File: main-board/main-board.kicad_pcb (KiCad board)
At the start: 4 copper layers, 142.9 x 86.4 mm, 175 parts, among them J1 BOOT, J10 8P8CDouble, J11 Qwiic, J12 Qwiic, J13 Qwiic, J14 YELLOW, J15 GREEN, J2 USB Header, J3 JTAG, J4 5V Input, J5 StatusPanel, J6 Magjack, J7 8P8CDouble, J8 8P8CDouble, J9 8P8CDouble, Q1 N Channel, Q10 N Channel, Q11 N Channel, Q12 N Channel, Q13 P Channel, Q14 P Channel, Q15 P Channel, Q16 P Channel, Q17 P Channel, Q2 N Channel, Q3 N Channel, Q4 N Channel, Q5 P Channel, Q6 P Channel, Q7 P Channel, Q8 P Channel, Q9 N Channel, U1 STM32H743ZITx, U10 ISL83490, U11 ISL83490, U12 ISL83490, U2 USBLC6-2SC6, U3 3.3V Reg, U4 KSZ8041MLL, U5 ISL83490, U6 ISL83490, U7 ISL83490, U8 ISL83490, U9 ISL83490, X1 20MHz Oscillator, X2 25MHz Oscillator

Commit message: Swap power filter caps, tighten up trace routing
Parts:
- C47: footprint Capacitors_SMD:CP_Elec_5x4.5 -> Capacitors_SMD:CP_Elec_4x4.5
- C48: footprint Capacitors_SMD:CP_Elec_4x4.5 -> Capacitors_SMD:CP_Elec_5x5.3
- moved C1 17.1 mm to (154.7, 109.5)
- moved R50 3.90 mm to (198.8, 130.6)
- moved R51 3.90 mm to (198.8, 126.5)
- moved J14 3.90 mm to (203.3, 129.5)
- moved J15 3.90 mm to (203.3, 125.9)
- moved C29 3.34 mm to (202.3, 122.4), turned to 180 degrees
- moved J6 1.78 mm to (198.9, 115.6)
- moved C3 1.52 mm to (145.0, 106.2)
- moved C31 1.40 mm to (197.4, 123.6)
- moved FB5 1.40 mm to (194.3, 121.3)
- moved C30 1.40 mm to (197.4, 121.4)
- moved C25 0.99 mm to (167.4, 114.2)
- moved FB3 0.99 mm to (165.1, 114.2)
- moved C2 0.89 mm to (141.4, 106.2)
- moved FB2 0.18 mm to (181.2, 121.8)
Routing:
- net /I2C2_SDA: track 83.1 -> 69.3 mm
- net Net-(C30-Pad1): track 16.1 -> 24.7 mm
- net /JACK_YEL_CATH: track 18.1 -> 23.9 mm
- net /ETH_TXD0: track 53.3 -> 48.5 mm
- net /UART7_RX: track 42.1 -> 46.3 mm
- net /I2C2_SCL: track 72.0 -> 76.0 mm
- net /VBUS_SENSE: track 67.3 -> 71.0 mm, vias 0 -> 2
- net GND: track 329.3 -> 325.9 mm, vias 60 -> 58
- net /LINK2_Y: track 20.0 -> 22.8 mm
- net +3V3: track 86.1 -> 83.6 mm, vias 24 -> 23
- net /JACK_GRN_CATH: track 11.6 -> 9.20 mm
- net Net-(C32-Pad1): track 9.83 -> 7.97 mm
- net /ETH_LED0: track 31.2 -> 29.4 mm, vias 2 -> 0
- net /ETH_RD-: track 18.5 -> 20.3 mm
- net /ETH_TXD1: track 52.5 -> 50.8 mm
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
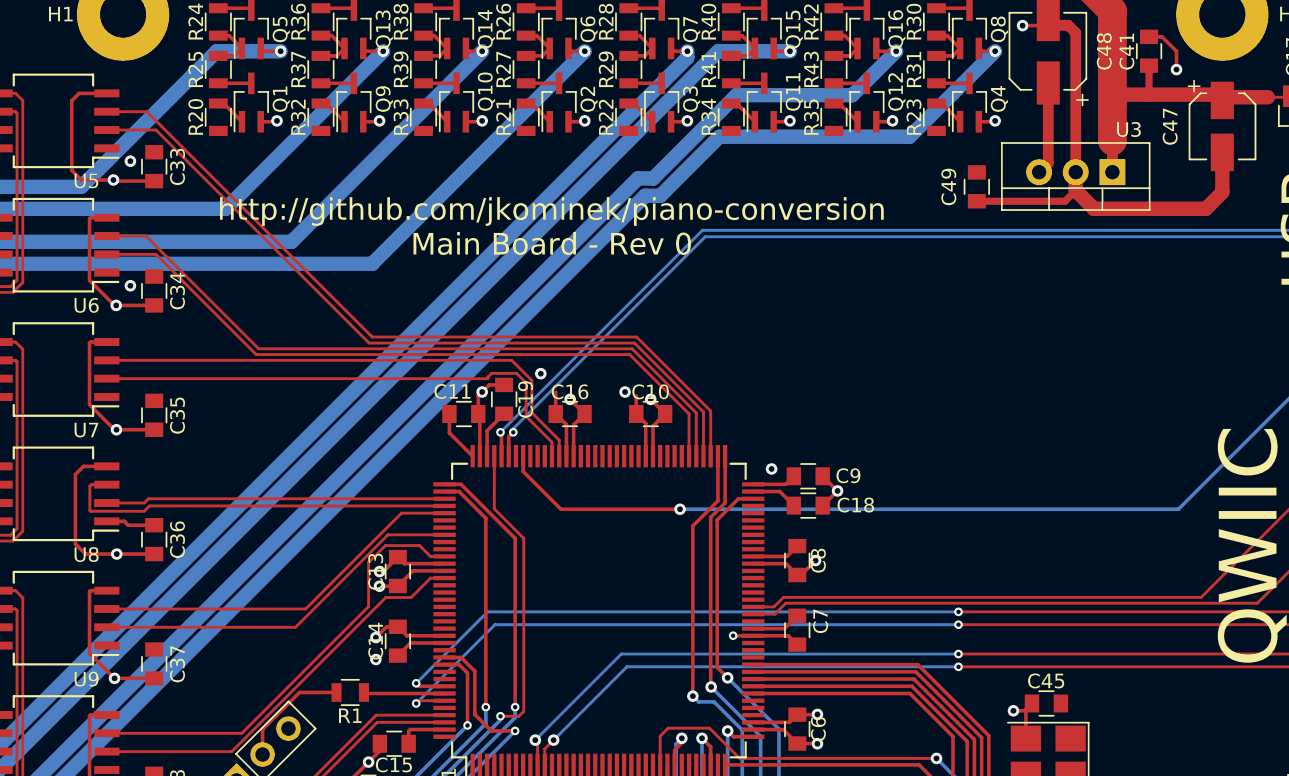
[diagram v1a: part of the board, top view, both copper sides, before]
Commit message: GPIO control lines for the MOSFET array
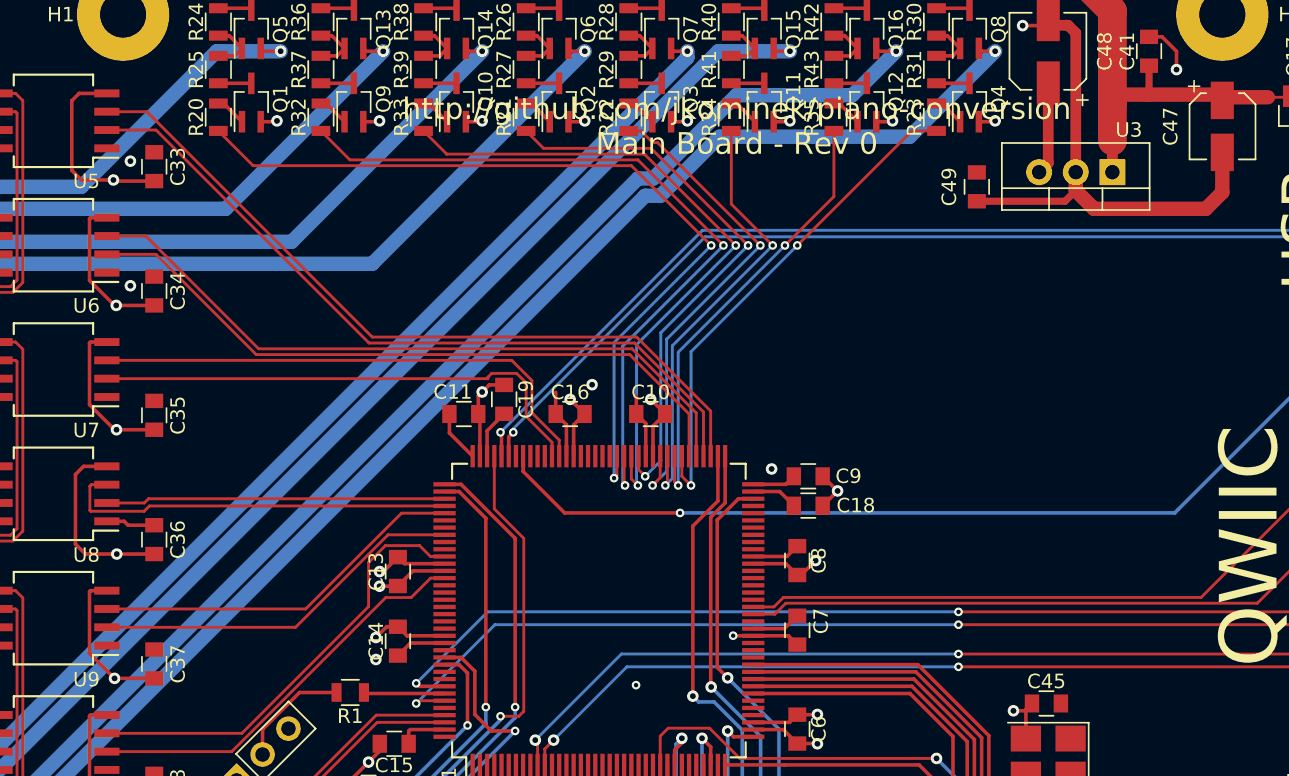
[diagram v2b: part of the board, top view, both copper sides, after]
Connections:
- R20 pad 2: (no net) -> /PWR1_CTRL
- R21 pad 2: (no net) -> /PWR3_CTRL
- R22 pad 2: (no net) -> /PWR5_CTRL
- R23 pad 2: (no net) -> /PWR7_CTRL
- R32 pad 2: (no net) -> /PWR2_CTRL
- R33 pad 2: (no net) -> /PWR4_CTRL
- R34 pad 2: (no net) -> /PWR6_CTRL
- R35 pad 2: (no net) -> /PWR8_CTRL
- U1 pad 79: (no net) -> /PWR7_CTRL
- U1 pad 80: (no net) -> /PWR8_CTRL
- U1 pad 81: (no net) -> /PWR6_CTRL
- U1 pad 82: (no net) -> /PWR5_CTRL
- U1 pad 85: (no net) -> /PWR3_CTRL
- U1 pad 86: (no net) -> /PWR4_CTRL
- U1 pad 87: (no net) -> /PWR2_CTRL
- U1 pad 88: (no net) -> /PWR1_CTRL
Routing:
- net /PWR1_CTRL: track 0.00 -> 58.0 mm, vias 0 -> 2
- net /PWR2_CTRL: track 0.00 -> 53.2 mm, vias 0 -> 2
- net /PWR4_CTRL: track 0.00 -> 46.7 mm, vias 0 -> 2
- net /PWR3_CTRL: track 0.00 -> 39.2 mm, vias 0 -> 2
- net /PWR7_CTRL: track 0.00 -> 34.9 mm, vias 0 -> 2
- net /PWR5_CTRL: track 0.00 -> 34.4 mm, vias 0 -> 2
- net /PWR8_CTRL: track 0.00 -> 31.2 mm, vias 0 -> 2
- net /PWR6_CTRL: track 0.00 -> 30.9 mm, vias 0 -> 2
- net GND: vias 58 -> 59
- net +3V3: vias 23 -> 22

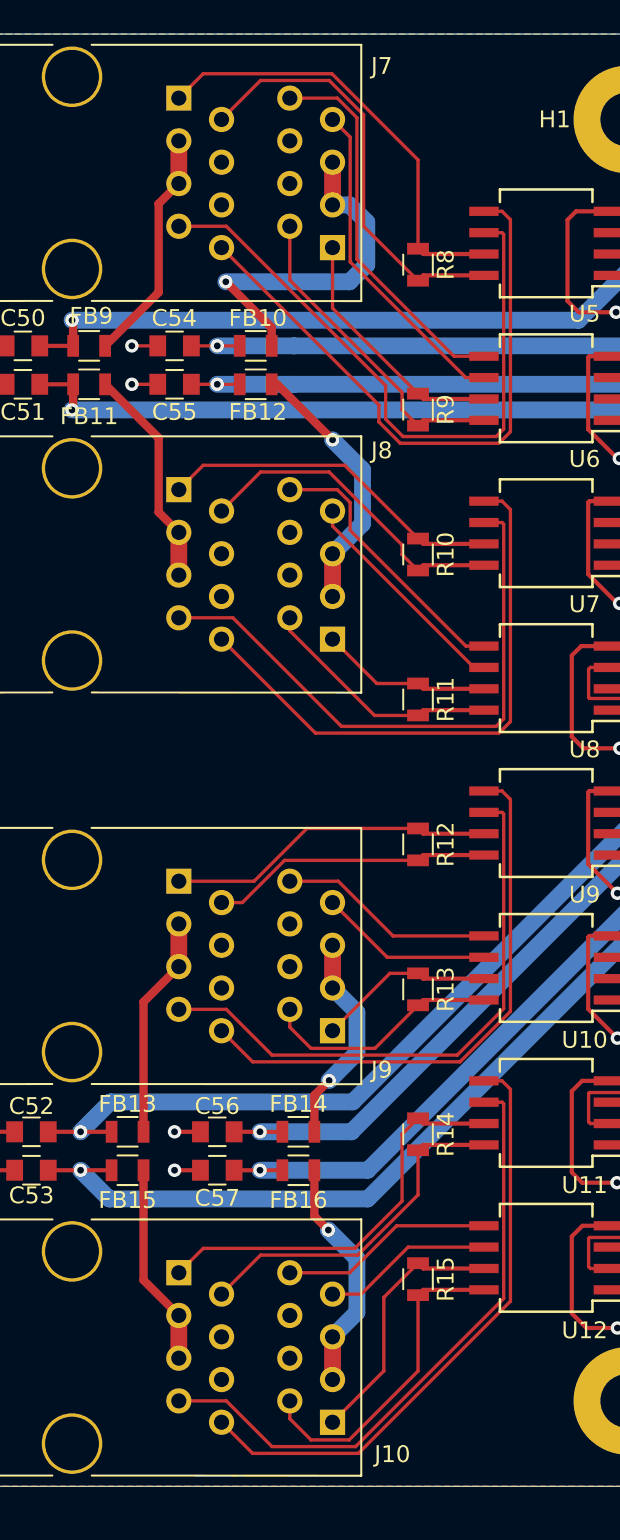
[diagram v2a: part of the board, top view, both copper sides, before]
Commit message: Correct RS485 Z/Y pin swap
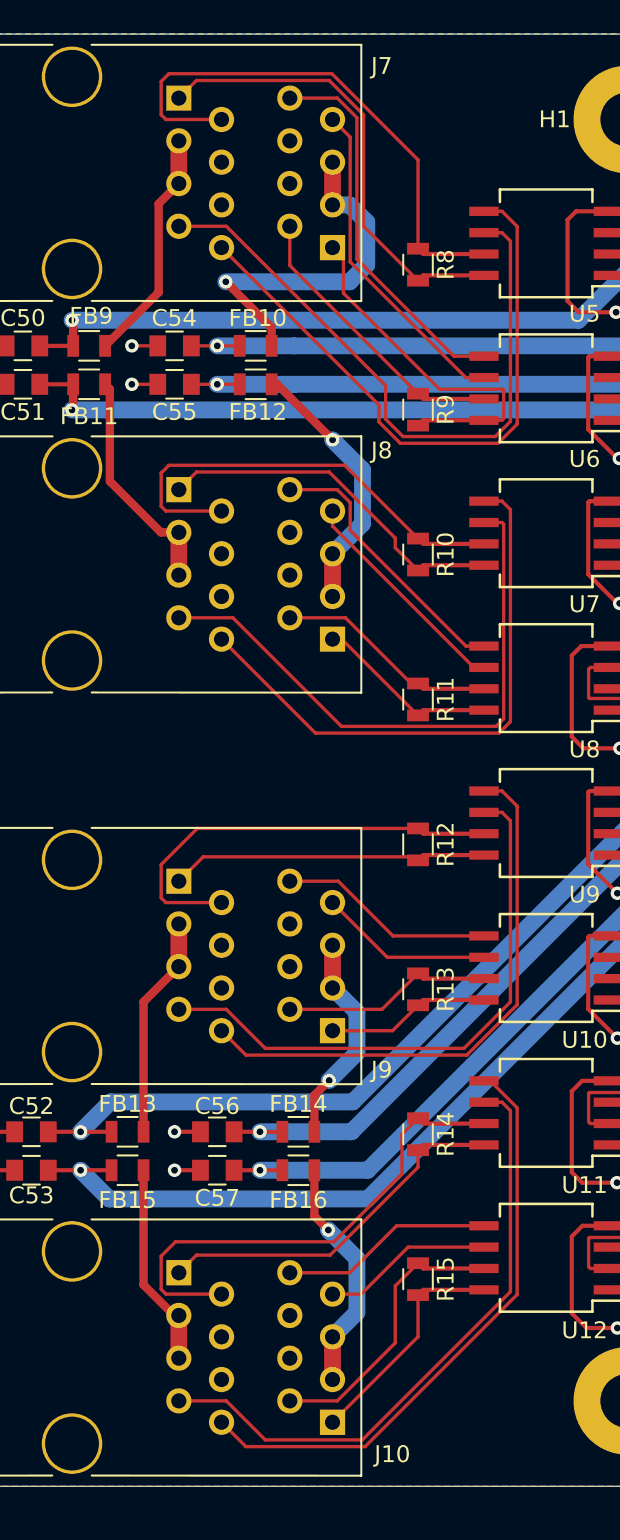
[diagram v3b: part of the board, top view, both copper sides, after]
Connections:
- J10 pad 1: /LINK7_B -> /LINK7_A
- J10 pad 10: /LINK8_A -> /LINK8_B
- J10 pad 2: /LINK7_A -> /LINK7_B
- J10 pad 9: /LINK8_B -> /LINK8_A
- J7 pad 1: /LINK1_B -> /LINK1_A
- J7 pad 10: /LINK2_A -> /LINK2_B
- J7 pad 2: /LINK1_A -> /LINK1_B
- J7 pad 9: /LINK2_B -> /LINK2_A
- J8 pad 1: /LINK3_B -> /LINK3_A
- J8 pad 10: /LINK4_A -> /LINK4_B
- J8 pad 2: /LINK3_A -> /LINK3_B
- J8 pad 9: /LINK4_B -> /LINK4_A
- J9 pad 1: /LINK5_B -> /LINK5_A
- J9 pad 10: /LINK6_A -> /LINK6_B
- J9 pad 2: /LINK5_A -> /LINK5_B
- J9 pad 9: /LINK6_B -> /LINK6_A
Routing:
- net /LINK1_B: track 26.3 -> 32.6 mm
- net /LINK5_B: track 19.6 -> 25.9 mm
- net /LINK3_B: track 20.7 -> 27.0 mm
- net /LINK8_A: track 19.5 -> 13.7 mm
- net /LINK7_B: track 24.4 -> 29.8 mm
- net /LINK6_A: track 14.3 -> 9.76 mm
- net /LINK4_A: track 14.5 -> 11.0 mm
- net /LINK4_B: track 10.2 -> 13.3 mm
- net /LINK2_A: track 19.1 -> 21.9 mm
- net /LINK2_B: track 14.8 -> 17.2 mm
- net /LINK5_A: track 16.8 -> 19.0 mm
- net /LINK3_A: track 19.5 -> 21.5 mm
- net /LINK1_A: track 25.5 -> 27.5 mm
- net /LINK6_B: track 10.5 -> 12.6 mm
- net /LINK8_B: track 15.6 -> 17.1 mm
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
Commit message: Fix UART and I2C pin errors. Add ETH INTRP and RXER pins.
Various vias added, and passives packed in better around the ethernet.
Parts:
- moved R47 58.3 mm to (180.6, 72.0), turned to 270 degrees
- moved R48 57.0 mm to (183.1, 72.0), turned to 270 degrees
- moved R49 56.1 mm to (185.6, 72.0), turned to 270 degrees
- moved J5 51.3 mm to (180.5, 78.1)
- moved R44 49.7 mm to (180.5, 82.9), turned to 270 degrees
- moved R45 47.6 mm to (183.1, 82.9), turned to 270 degrees
- moved R46 45.8 mm to (185.6, 82.9), turned to 270 degrees
- moved Q17 5.52 mm to (198.5, 53.1), turned to 0 degrees
- moved J4 3.76 mm to (208.2, 55.5), turned to 90 degrees
- moved FB2 2.32 mm to (181.6, 119.5)
- moved R6 1.79 mm to (176.3, 122.0), turned to 180 degrees
- moved C27 1.50 mm to (187.5, 115.9)
- moved C24 1.50 mm to (189.6, 115.9)
- moved C49 1.43 mm to (172.2, 62.1), turned to 180 degrees
- moved C26 1.21 mm to (184.7, 118.8)
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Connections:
- U1 pad 111: /UART4_RX -> /UART4_TX
- U1 pad 112: /UART4_TX -> /UART4_RX
- U1 pad 136: (no net) -> /I2C1_SCL
- U1 pad 139: /I2C1_SCL -> (no net)
- U1 pad 41: (no net) -> /ETH_RXER
- U1 pad 42: (no net) -> /ETH_INTRP
- U4 pad 29: (no net) -> /ETH_RXER
- U4 pad 32: (no net) -> /ETH_INTRP
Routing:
- net /ETH_INTRP: track 0.00 -> 28.9 mm, vias 0 -> 2
- net /NRST: track 53.0 -> 78.2 mm, vias 0 -> 2
- net /ETH_RXER: track 0.00 -> 22.3 mm, vias 0 -> 2
- net GND: track 325.9 -> 311.0 mm, vias 59 -> 65
- net +3V3: track 83.6 -> 73.2 mm, vias 22 -> 47
- net Net-(J5-Pad6): track 9.92 -> 2.64 mm
- net Net-(C20-Pad2): track 20.7 -> 14.8 mm
- net Net-(J5-Pad4): track 7.80 -> 2.64 mm
- net /LEDSTATUS: track 48.8 -> 53.2 mm, vias 0 -> 2
- net Net-(C24-Pad1): track 33.3 -> 28.9 mm
- net +5V: track 125.7 -> 130.0 mm
- net /ETH_TD+: track 21.8 -> 25.7 mm, vias 1 -> 0
- net /UART4_TX: track 27.7 -> 23.8 mm
- net Net-(J5-Pad3): track 6.57 -> 3.83 mm
- net Net-(J5-Pad2): track 5.13 -> 2.66 mm
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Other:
- board text added: "<-Gnds"
- board text added: "I2C1"
- board text added: "I2C2"
- board text added: "I2C4"
- board text removed: "[Gnd]"

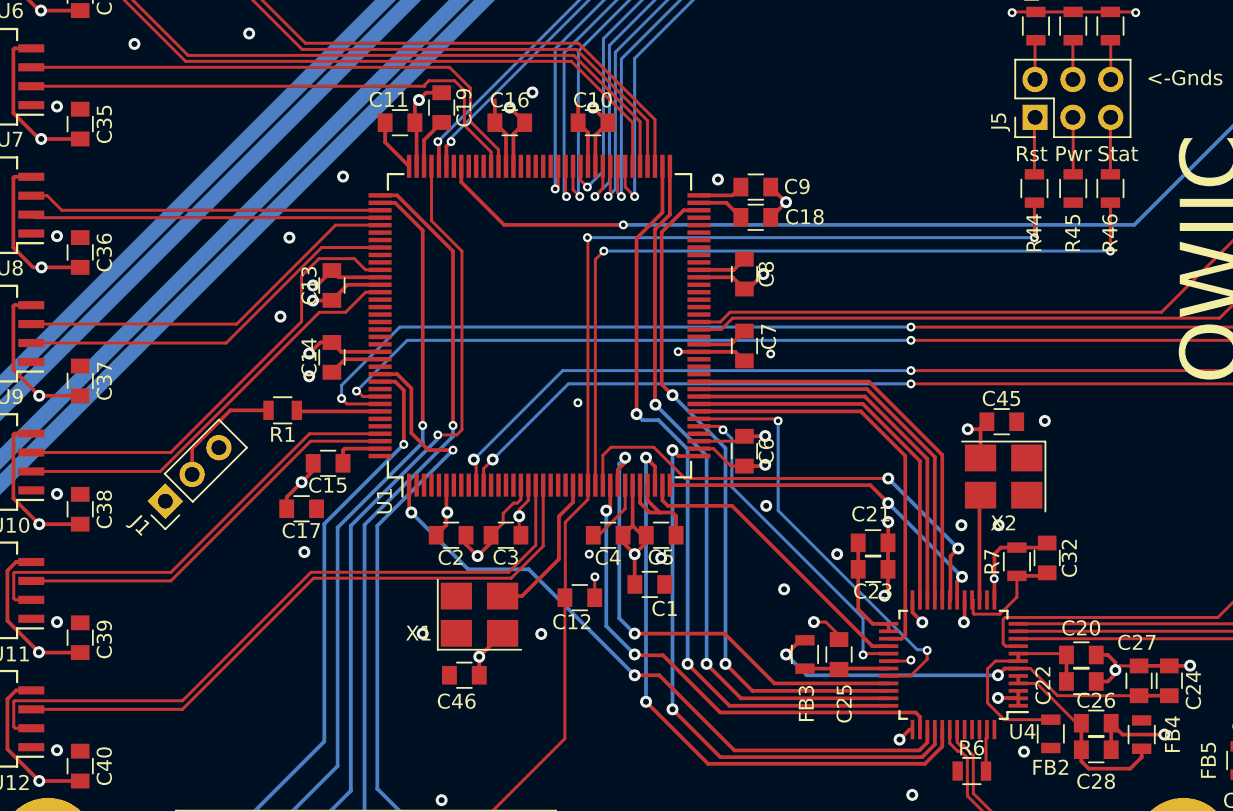
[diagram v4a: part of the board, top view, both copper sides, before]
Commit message: Include a SPI flash
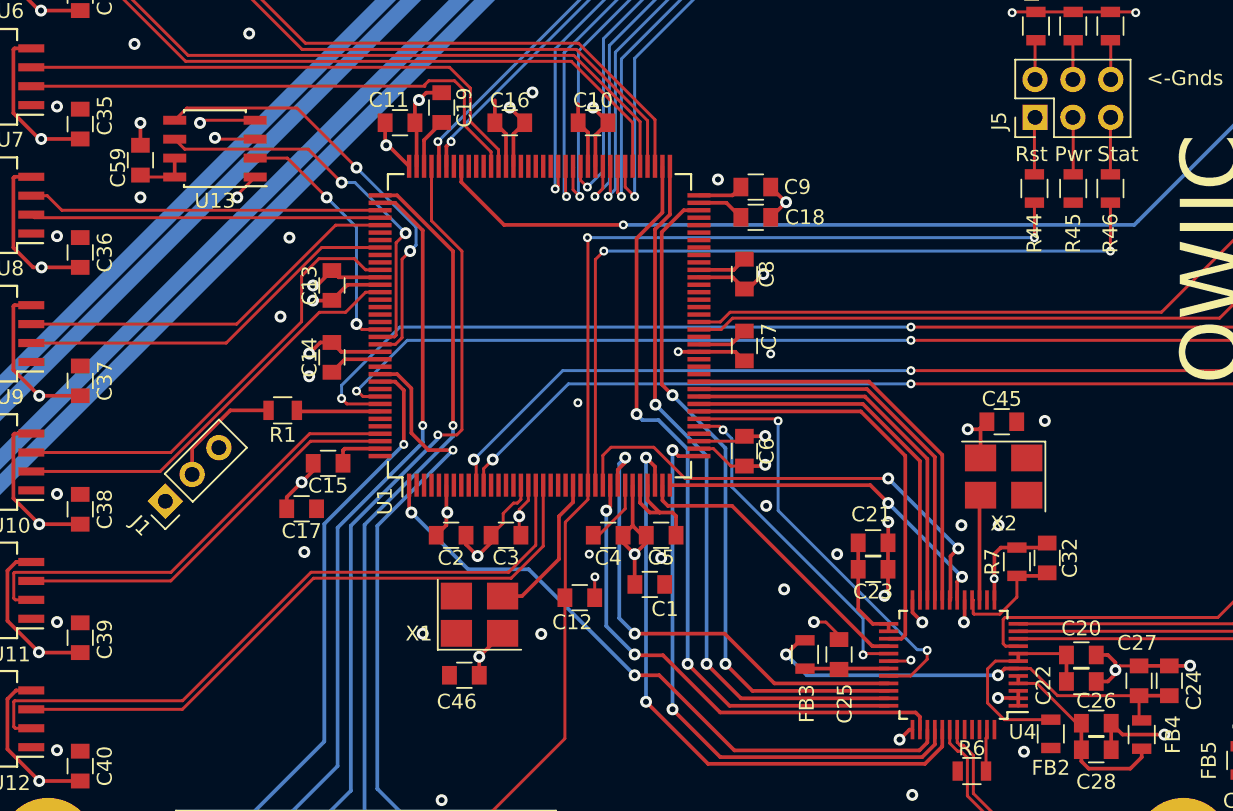
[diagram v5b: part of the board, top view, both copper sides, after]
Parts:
- added C59: DC6, Capacitors_SMD:C_0805, F.Cu at (120.5, 81.0)
- added U13: W25Q80DVSNIG, Housings_SOIC:SOIC-8_3.9x4.9mm_Pitch1.27mm, F.Cu at (125.5, 80.2)
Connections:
- U1 pad 127: (no net) -> /SPI6_MISO
- U1 pad 128: (no net) -> /SPI6_SCK
- U1 pad 129: (no net) -> /SPI6_MOSI
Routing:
- net /SPI6_MOSI: track 0.00 -> 29.3 mm, vias 0 -> 2
- net /SPI6_SCK: track 0.00 -> 26.4 mm, vias 0 -> 2
- net /SPI6_MISO: track 0.00 -> 17.0 mm, vias 0 -> 2
- net GND: track 311.0 -> 318.2 mm, vias 65 -> 68
- net +3V3: track 73.2 -> 79.6 mm, vias 47 -> 49
- net Net-(C24-Pad1): track 28.9 -> 30.6 mm
